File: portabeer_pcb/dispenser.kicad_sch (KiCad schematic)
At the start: 36 parts, among them J15 Conn_01x03, J16 Conn_01x03, M1 Air pump, M3 Water pump, M7 Fan_4pin, Q6 SiS454DN, Q7 AO3400A, Q8 AO3400A

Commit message: electronics diagram and schematic
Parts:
- C67: footprint (none) -> Capacitor_THT:CP_Radial_D8.0mm_P3.50mm
- C73, C74: footprint (none) -> Capacitor_THT:CP_Radial_D6.3mm_P2.50mm
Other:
- company: (none) -> ©2024 Luca Anastasio
- title: (none) -> Beerpak
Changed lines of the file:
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@@
 	(generator_version "8.0")
 	(paper "A4")
+	(title_block
+		(title "Beerpak")
+		(company "©2024 Luca Anastasio")
+	)
 	(junction
 		(at 160.02 176.53)
@@
 			)
 		)
-		(property "Footprint" ""
+		(property "Footprint" "Capacitor_THT:CP_Radial_D6.3mm_P2.50mm"
 			(at 247.3452 63.5 0)
 			(effects
@@
 			)
 		)
-		(property "Footprint" ""
+		(property "Footprint" "Capacitor_THT:CP_Radial_D8.0mm_P3.50mm"
 			(at 134.3152 134.62 0)
 			(effects
@@
 			)
 		)
-		(property "Footprint" ""
+		(property "Footprint" "Capacitor_THT:CP_Radial_D6.3mm_P2.50mm"
 			(at 242.2652 135.89 0)
 			(effects

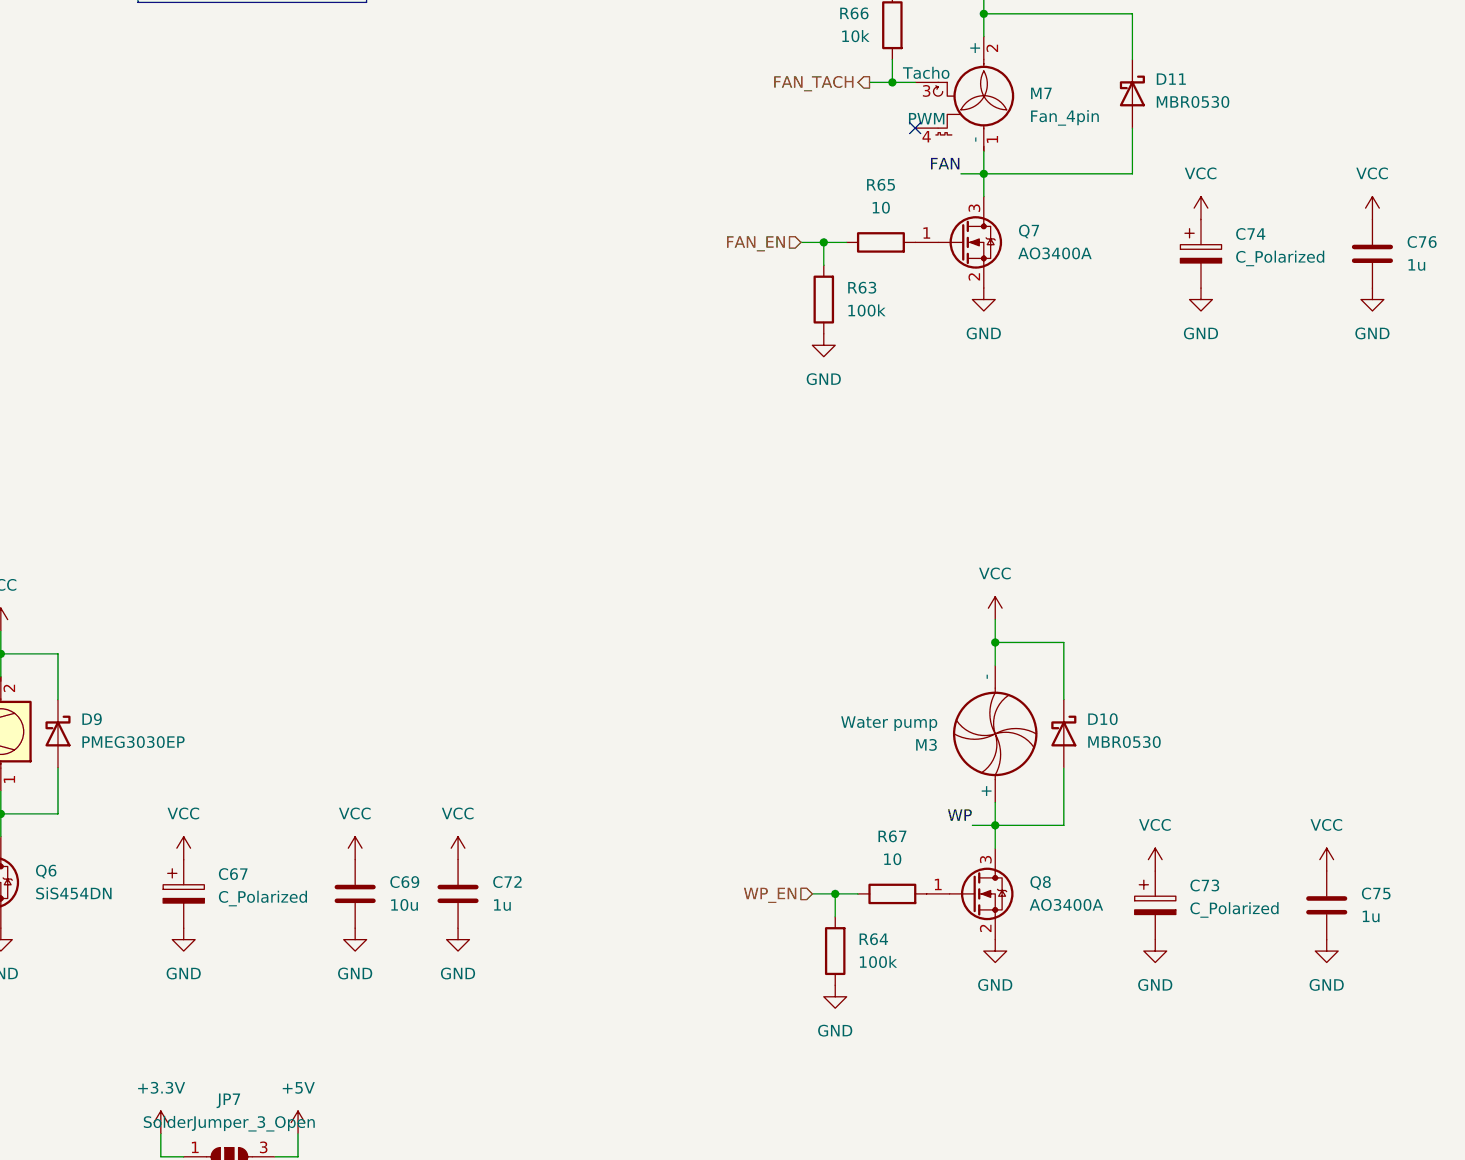
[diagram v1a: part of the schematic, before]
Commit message: added 3d models, started layout
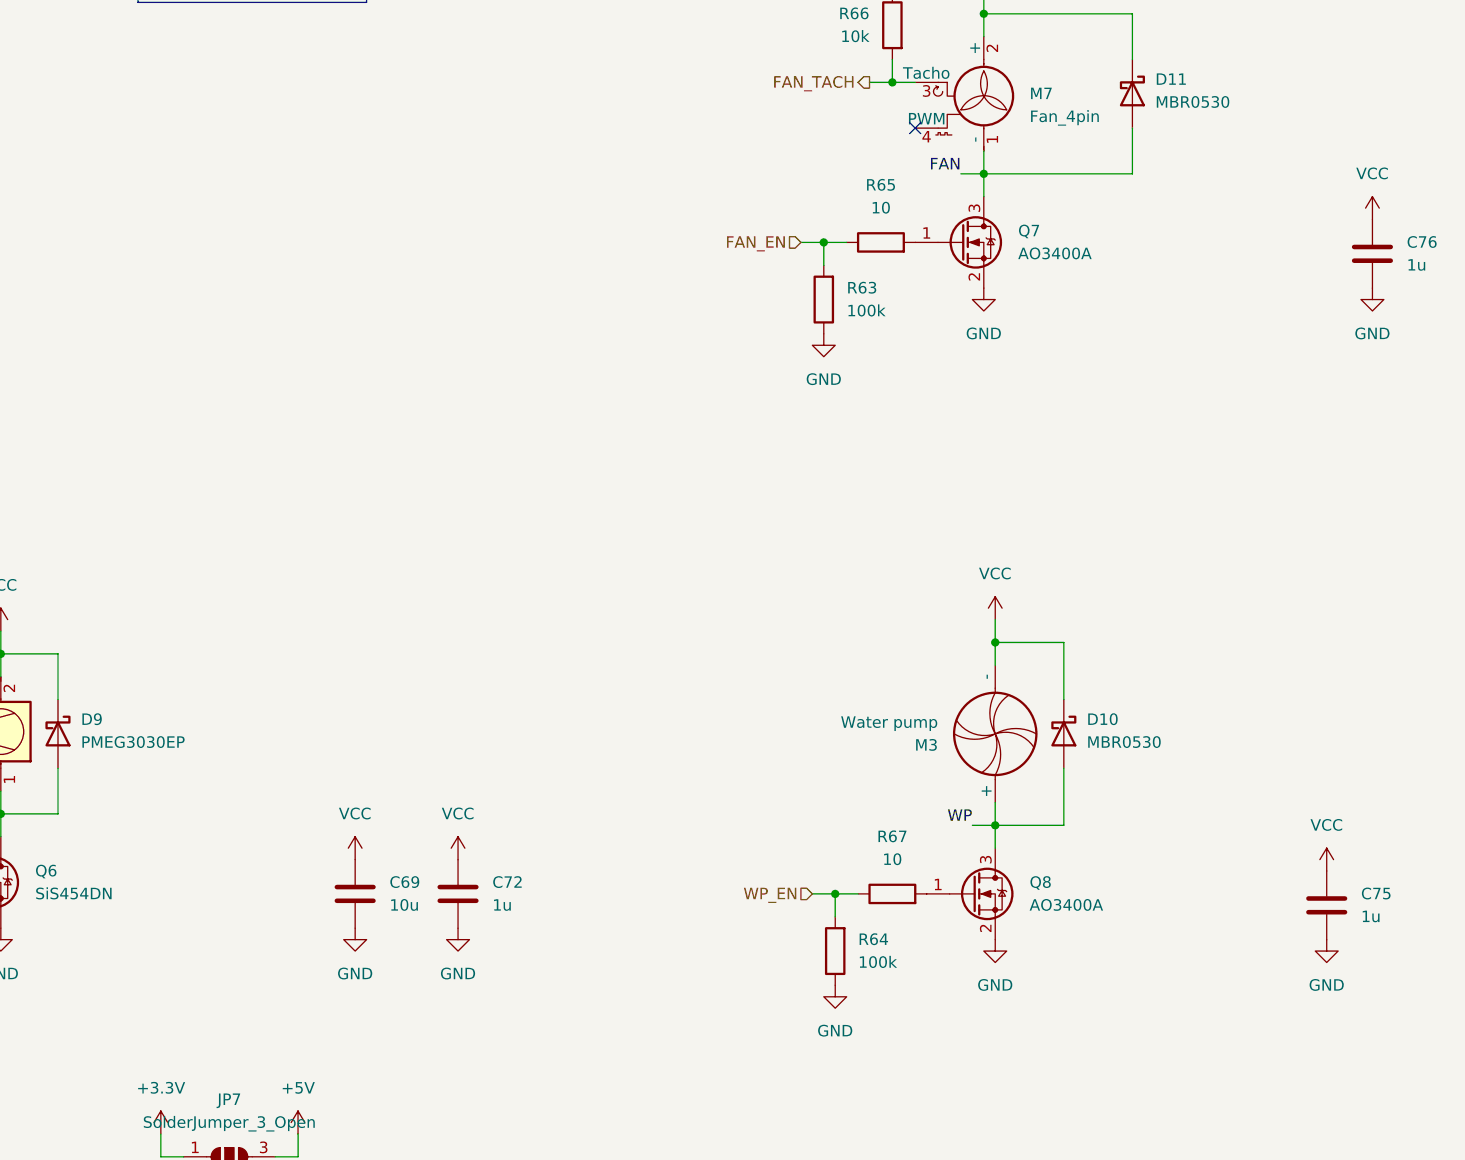
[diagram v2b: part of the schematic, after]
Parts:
- removed C67: C_Polarized, Capacitor_THT:CP_Radial_D8.0mm_P3.50mm, symbol Device:C_Polarized
- removed C73, C74: C_Polarized, Capacitor_THT:CP_Radial_D6.3mm_P2.50mm, symbol Device:C_Polarized
- Q6: footprint Package_SO:Vishay_PowerPAK_1212-8_Single -> portabeer:Vishay_PowerPAK_1212-8_Single

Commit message: working
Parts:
- removed M3: Water pump, portabeer:Molex_KK-254_1x02_P2.54mm_Horizontal, symbol Motor:Fan_ALT
- removed M7: Fan_4pin, portabeer:Molex_KK-254_1x03_P2.54mm_Horizontal, symbol Motor:Fan_4pin
- added J19: FAN, Connector_Molex:Molex_KK-254_AE-6410-03A_1x03_P2.54mm_Vertical, symbol Connector_Generic:Conn_01x03
- added J21: WATER PUMP, Connector_Molex:Molex_KK-254_AE-6410-02A_1x02_P2.54mm_Vertical, symbol Connector_Generic:Conn_01x02
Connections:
- net FAN: now also J19.1 (Pin_1)
- net FAN_TACH: now also J19.3 (Pin_3)
- net VCC: now also J19.2 (Pin_2), J21.2 (Pin_2)
- net WP: now also J21.1 (Pin_1)
- no-connect marks 1 -> 0
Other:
- moved on the sheet: R66

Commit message: partial routing
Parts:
- removed C65: C, Capacitor_SMD:C_0603_1608Metric, symbol Device:C
- removed C69: 10u, Capacitor_SMD:C_1206_3216Metric, symbol Device:C
- removed C70: 1n, Capacitor_SMD:C_0603_1608Metric, symbol Device:C
- removed C72: 1u, Capacitor_SMD:C_0603_1608Metric, symbol Device:C
- removed D9: PMEG3030EP, Diode_SMD:D_SOD-128, symbol Device:D_Schottky
- removed J16: Conn_01x03, Connector_JST:JST_XH_B3B-XH-A_1x03_P2.50mm_Vertical, symbol Connector_Generic:Conn_01x03
- removed JP7: SolderJumper_3_Open, Jumper:SolderJumper-3_P1.3mm_Open_RoundedPad1.0x1.5mm, symbol Jumper:SolderJumper_3_Open
- removed M1: Air pump, Connector_Phoenix_MC:PhoenixContact_MC_1,5_2-G-3.81_1x02_P3.81mm_Horizontal, symbol Motor:Fan_IEC60617
- removed Q6: SiS454DN, portabeer:Vishay_PowerPAK_1212-8_Single, symbol Transistor_FET:SiS454DN
- removed R60: 10, Resistor_SMD:R_0603_1608Metric, symbol Device:R
- removed R61: 1k, Resistor_SMD:R_0603_1608Metric, symbol Device:R
- removed R62: 1.96k, Resistor_SMD:R_0603_1608Metric, symbol Device:R
- added JP9: SolderJumper_2_Open, Jumper:SolderJumper-2_P1.3mm_Open_RoundedPad1.0x1.5mm, symbol Jumper:SolderJumper_2_Open
- PE1: symbol Device:PeltierElement -> Connector:Screw_Terminal_01x02
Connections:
- net GND: now also JP9.1 (A); no longer R57.1
- new net: JP9.2 (B), R57.1
